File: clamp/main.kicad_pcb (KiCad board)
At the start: 2 copper layers, 76 parts, among them P1 CONN_01X12, P2 CONN_01X15, P3 CONN_01X03, P4 CONN_01X06, Q1 2N3904, U1 LM741, U12 LTZ1000, U13 LM741, U14 LM741, U2 LM741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

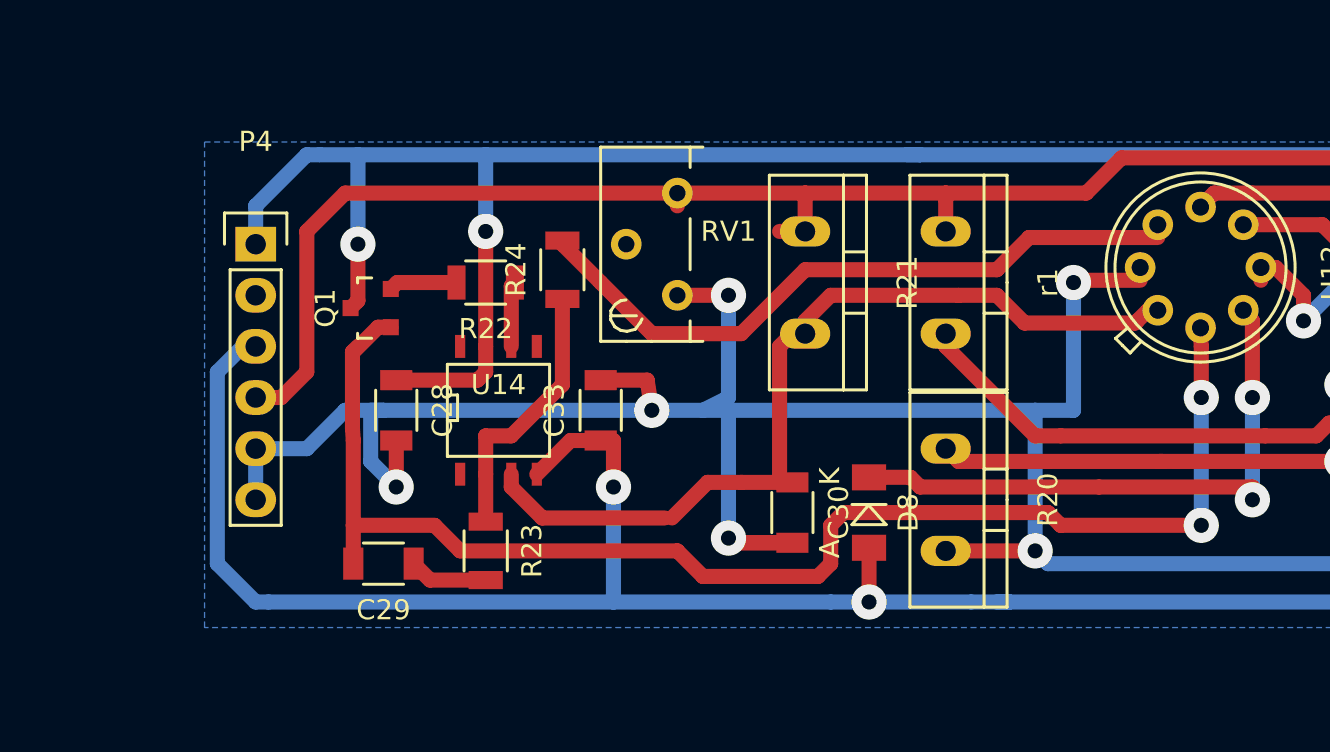
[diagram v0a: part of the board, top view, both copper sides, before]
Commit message: add resistor divider in place of pot
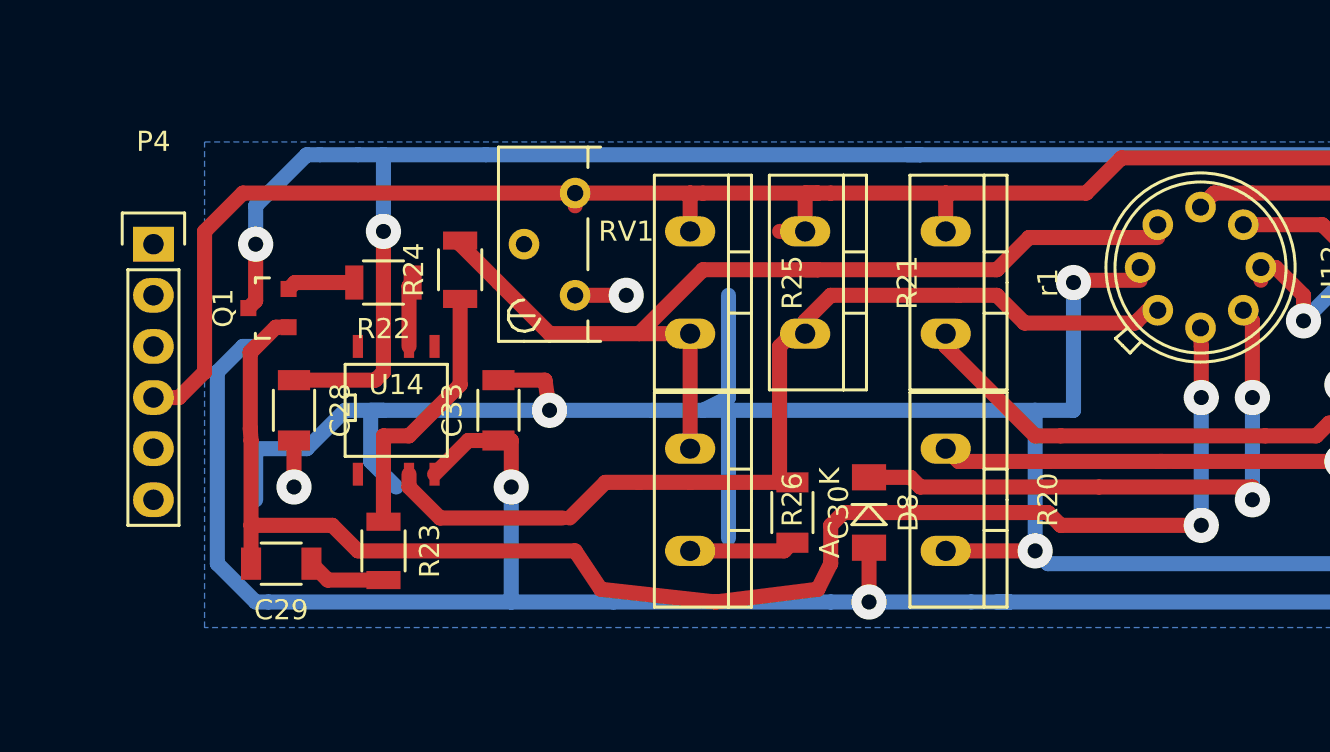
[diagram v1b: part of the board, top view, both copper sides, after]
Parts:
- added R25: 12k, Resistors_ThroughHole:Resistor_TO-220_Vertical, F.Cu at (202.6, 46.4)
- added R26: 1k, Resistors_ThroughHole:Resistor_TO-220_Vertical, F.Cu at (202.6, 57.1)
- moved C28 5.08 mm to (182.9, 52.7)
- moved C33 5.08 mm to (193.0, 52.7)
- moved R22 5.08 mm to (187.3, 46.4)
- moved R23 5.08 mm to (187.3, 59.7)
- moved R24 5.08 mm to (191.1, 45.7)
- moved RV1 5.08 mm to (196.8, 47.0)
- moved C29 5.08 mm to (182.2, 60.3)
- moved P4 5.08 mm to (175.9, 44.5)
- moved Q1 5.08 mm to (181.6, 47.6)
- moved U14 5.08 mm to (188.0, 52.7)
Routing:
- net Net-(R24-Pad2): track 33.6 -> 47.6 mm
- net REF: track 98.1 -> 105.7 mm
- net Net-(C29-Pad2): track 69.1 -> 75.3 mm
- net Net-(C30-Pad1): track 43.4 -> 48.5 mm
- net +VE: track 385.3 -> 380.8 mm
- net GND: track 207.9 -> 207.6 mm, vias 17 -> 16

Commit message: update
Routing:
- net GND: track 207.6 -> 219.7 mm
- net +VE: track 380.8 -> 391.7 mm
- net -VE: track 362.7 -> 365.7 mm
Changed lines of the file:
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@@
   (general
     (links 171)
-    (no_connects 87)
+    (no_connects 82)
     (area -5.909001 -6.355 253.23 151.352002)
     (thickness 1.6)
     (drawings 13)
-    (tracks 524)
+    (tracks 534)
     (zones 0)
     (modules 78)
@@
     (effects (font (size 1.5 1.5) (thickness 0.3)))
   )
+  (segment (start 184.15 40.005) (end 179.07 40.005) (width 0.75) (layer B.Cu) (net 1))
+  (segment (start 175.895 43.18) (end 175.895 44.45) (width 0.75) (layer B.Cu) (net 1))
+  (segment (start 179.07 40.005) (end 175.895 43.18) (width 0.75) (layer B.Cu) (net 1))
   (segment (start 187.325 40.005) (end 187.325 43.815) (width 0.75) (layer B.Cu) (net 1))
   (via (at 187.325 43.815) (size 1.75) (drill 0.75) (layers F.Cu B.Cu) (net 1))
@@
   (via (at 121.92 86.36) (size 1.75) (drill 0.75) (layers F.Cu B.Cu) (net 1))
   (segment (start 121.92 86.36) (end 166.624 86.36) (width 0.75) (layer B.Cu) (net 1))
+  (segment (start 179.07 52.07) (end 179.07 50.165) (width 0.75) (layer B.Cu) (net 2))
+  (segment (start 178.435 49.53) (end 175.895 49.53) (width 0.75) (layer B.Cu) (net 2))
+  (segment (start 179.07 50.165) (end 178.435 49.53) (width 0.75) (layer B.Cu) (net 2))
   (segment (start 193.675 62.23) (end 193.675 56.515) (width 0.75) (layer B.Cu) (net 2))
   (via (at 193.675 56.515) (size 1.75) (drill 0.75) (layers F.Cu B.Cu) (net 2))
   (segment (start 193.675 56.515) (end 193.675 54.205) (width 0.75) (layer F.Cu) (net 2))
-  (segment (start 180.975 49.53) (end 180.34 49.53) (width 0.75) (layer B.Cu) (net 2))
-  (segment (start 180.34 49.53) (end 179.07 50.8) (width 0.75) (layer B.Cu) (net 2))
-  (segment (start 179.07 50.8) (end 179.07 60.325) (width 0.75) (layer B.Cu) (net 2))
+  (segment (start 179.07 50.8) (end 179.07 52.07) (width 0.75) (layer B.Cu) (net 2))
+  (segment (start 179.07 52.07) (end 179.07 60.325) (width 0.75) (layer B.Cu) (net 2))
   (segment (start 179.07 60.325) (end 180.975 62.23) (width 0.75) (layer B.Cu) (net 2))
   (segment (start 180.975 62.23) (end 181.61 62.23) (width 0.75) (layer B.Cu) (net 2))
-  (segment (start 198.755 62.23) (end 193.675 62.23) (width 0.75) (layer B.Cu) (net 2))
+  (segment (start 207.01 62.23) (end 193.675 62.23) (width 0.75) (layer B.Cu) (net 2))
   (segment (start 193.675 62.23) (end 181.61 62.23) (width 0.75) (layer B.Cu) (net 2))
-  (segment (start 209.55 62.23) (end 198.755 62.23) (width 0.75) (layer B.Cu) (net 2))
+  (segment (start 208.28 62.23) (end 207.01 62.23) (width 0.75) (layer B.Cu) (net 2))
   (segment (start 248.92 53.34) (end 248.92 62.23) (width 0.75) (layer F.Cu) (net 2))
   (via (at 248.92 62.23) (size 1.75) (drill 0.75) (layers F.Cu B.Cu) (net 2))
@@
   (segment (start 249.555 52.705) (end 249.555 51.665) (width 0.75) (layer F.Cu) (net 2))
   (segment (start 248.92 53.34) (end 249.555 52.705) (width 0.75) (layer F.Cu) (net 2))
-  (segment (start 211.455 62.23) (end 209.55 62.23) (width 0.75) (layer B.Cu) (net 2))
+  (segment (start 211.455 62.23) (end 208.28 62.23) (width 0.75) (layer B.Cu) (net 2))
   (segment (start 193.675 54.205) (end 191.54 54.205) (width 0.75) (layer F.Cu) (net 2))
   (segment (start 191.54 54.205) (end 189.865 55.88) (width 0.75) (layer F.Cu) (net 2))
@@
   (segment (start 165.862 96.012) (end 165.862 96.52) (width 0.75) (layer B.Cu) (net 2))
   (segment (start 157.132 104.775) (end 160.30194 104.648) (width 0.75) (layer F.Cu) (net 3) (status 30))
+  (segment (start 175.895 46.99) (end 175.26 46.99) (width 0.75) (layer B.Cu) (net 4))
+  (segment (start 175.26 46.99) (end 173.99 48.26) (width 0.75) (layer B.Cu) (net 4))
+  (segment (start 173.99 48.26) (end 173.99 52.705) (width 0.75) (layer B.Cu) (net 4))
+  (segment (start 173.99 52.705) (end 175.895 54.61) (width 0.75) (layer B.Cu) (net 4))
+  (segment (start 175.895 57.15) (end 175.895 54.61) (width 0.75) (layer B.Cu) (net 4))
   (segment (start 202.565 59.69) (end 207.24 59.69) (width 0.75) (layer F.Cu) (net 4))
   (segment (start 207.24 59.69) (end 207.645 59.285) (width 0.75) (layer F.Cu) (net 4))
@@
   (segment (start 217.805 45.72) (end 208.915 45.72) (width 0.75) (layer F.Cu) (net 33))
   (segment (start 191.135 44.45) (end 191.135 44.27) (width 0.75) (layer F.Cu) (net 33))
+  (segment (start 207.645 62.23) (end 209.55 60.325) (width 0.75) (layer F.Cu) (net 34))
+  (segment (start 227.965 58.42) (end 220.98 58.42) (width 0.75) (layer F.Cu) (net 34))
+  (via (at 227.965 52.07) (size 1.75) (drill 0.75) (layers F.Cu B.Cu) (net 34))
+  (segment (start 227.965 58.42) (end 227.965 52.07) (width 0.75) (layer B.Cu) (net 34))
+  (via (at 227.965 58.42) (size 1.75) (drill 0.75) (layers F.Cu B.Cu) (net 34))
+  (segment (start 209.55 60.325) (end 209.55 58.42) (width 0.75) (layer F.Cu) (net 34))
+  (segment (start 209.55 58.42) (end 210.185 57.785) (width 0.75) (layer F.Cu) (net 34))
+  (segment (start 210.185 57.785) (end 211.455 57.785) (width 0.75) (layer F.Cu) (net 34))
+  (segment (start 220.345 57.785) (end 211.455 57.785) (width 0.75) (layer F.Cu) (net 34))
+  (segment (start 220.98 58.42) (end 220.345 57.785) (width 0.75) (layer F.Cu) (net 34))
   (segment (start 182.61076 48.575) (end 181.97576 48.575) (width 0.75) (layer F.Cu) (net 34))
   (segment (start 181.97576 48.575) (end 180.70576 49.845) (width 0.75) (layer F.Cu) (net 34))
@@
   (segment (start 180.745 54.205) (end 180.745 58.42) (width 0.75) (layer F.Cu) (net 34))
   (segment (start 180.70576 53.60924) (end 180.745 54.205) (width 0.75) (layer F.Cu) (net 34))
-  (segment (start 203.835 62.23) (end 208.915 61.595) (width 0.75) (layer F.Cu) (net 34))
+  (segment (start 203.835 62.23) (end 207.645 62.23) (width 0.75) (layer F.Cu) (net 34))
   (segment (start 180.745 58.42) (end 184.785 58.42) (width 0.75) (layer F.Cu) (net 34))
-  (segment (start 208.915 61.595) (end 209.55 60.325) (width 0.75) (layer F.Cu) (net 34))
-  (segment (start 198.12 61.595) (end 203.835 62.23) (width 0.75) (layer F.Cu) (net 34))
-  (segment (start 196.85 59.69) (end 198.12 61.595) (width 0.75) (layer F.Cu) (net 34))
+  (segment (start 198.755 62.23) (end 203.835 62.23) (width 0.75) (layer F.Cu) (net 34))
+  (segment (start 196.85 59.69) (end 198.755 62.23) (width 0.75) (layer F.Cu) (net 34))
   (segment (start 186.055 59.69) (end 196.85 59.69) (width 0.75) (layer F.Cu) (net 34))
   (segment (start 184.785 58.42) (end 186.055 59.69) (width 0.75) (layer F.Cu) (net 34))
   (segment (start 180.745 58.42) (end 180.745 60.325) (width 0.75) (layer F.Cu) (net 34))
-  (segment (start 220.98 58.42) (end 220.345 57.785) (width 0.75) (layer F.Cu) (net 34))
-  (segment (start 220.345 57.785) (end 211.455 57.785) (width 0.75) (layer F.Cu) (net 34))
-  (segment (start 210.185 57.785) (end 211.455 57.785) (width 0.75) (layer F.Cu) (net 34))
-  (segment (start 209.55 58.42) (end 210.185 57.785) (width 0.75) (layer F.Cu) (net 34))
-  (segment (start 209.55 60.325) (end 209.55 58.42) (width 0.75) (layer F.Cu) (net 34))
-  (via (at 227.965 58.42) (size 1.75) (drill 0.75) (layers F.Cu B.Cu) (net 34))
-  (segment (start 227.965 58.42) (end 227.965 52.07) (width 0.75) (layer B.Cu) (net 34))
-  (via (at 227.965 52.07) (size 1.75) (drill 0.75) (layers F.Cu B.Cu) (net 34))
-  (segment (start 227.965 58.42) (end 220.98 58.42) (width 0.75) (layer F.Cu) (net 34))
   (segment (start 227.9275 48.6075) (end 227.9275 48.9325) (width 0.75) (layer F.Cu) (net 34) (status 30))
   (segment (start 227.9275 48.9325) (end 227.965 49.53) (width 0.75) (layer F.Cu) (net 34) (status 10))
@@
     (polygon
       (pts
-        (xy 252.095 63.5) (xy 178.435 63.5) (xy 178.435 39.37) (xy 252.095 39.37)
+        (xy 252.095 63.5) (xy 173.355 63.5) (xy 173.355 39.37) (xy 252.095 39.37)
       )
     )

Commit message: fix bodge
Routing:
- net Net-(R24-Pad2): track 47.6 -> 49.8 mm
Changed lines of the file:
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@@
   (general
     (links 171)
-    (no_connects 82)
-    (area -5.909001 -6.355 253.23 151.352002)
+    (no_connects 81)
+    (area 51.181667 26.645 253.23 151.352002)
     (thickness 1.6)
     (drawings 13)
-    (tracks 534)
+    (tracks 537)
     (zones 0)
     (modules 78)
@@
   (layers
     (0 F.Cu signal)
-    (31 B.Cu signal)
+    (31 B.Cu signal hide)
     (32 B.Adhes user)
     (33 F.Adhes user)
@@
   (segment (start 187.325 61.14) (end 184.56 61.14) (width 0.75) (layer F.Cu) (net 32))
   (segment (start 184.56 61.14) (end 183.745 60.325) (width 0.75) (layer F.Cu) (net 32))
-  (segment (start 202.565 48.895) (end 202.565 54.61) (width 0.75) (layer F.Cu) (net 33))
+  (segment (start 194.31 44.45) (end 191.315 44.45) (width 0.75) (layer F.Cu) (net 33) (status C00000))
+  (segment (start 191.315 44.45) (end 191.135 44.27) (width 0.75) (layer F.Cu) (net 33) (status C00000))
   (segment (start 200.025 48.895) (end 202.565 48.895) (width 0.75) (layer F.Cu) (net 33))
+  (segment (start 202.565 48.895) (end 202.565 46.355) (width 0.75) (layer F.Cu) (net 33))
+  (segment (start 202.565 48.895) (end 202.565 54.61) (width 0.75) (layer F.Cu) (net 33))
   (segment (start 208.915 45.72) (end 203.2 45.72) (width 0.75) (layer F.Cu) (net 33))
+  (segment (start 202.565 46.355) (end 203.2 45.72) (width 0.75) (layer F.Cu) (net 33))
   (segment (start 208.915 45.72) (end 208.28 45.72) (width 0.75) (layer F.Cu) (net 33))
   (segment (start 193.04 46.355) (end 191.135 44.45) (width 0.75) (layer F.Cu) (net 33))
   (segment (start 195.58 48.895) (end 200.025 48.895) (width 0.75) (layer F.Cu) (net 33))
-  (segment (start 200.025 48.895) (end 203.2 45.72) (width 0.75) (layer F.Cu) (net 33))
   (segment (start 193.04 46.355) (end 195.58 48.895) (width 0.75) (layer F.Cu) (net 33))
   (segment (start 225.8025 44.1175) (end 219.4075 44.1175) (width 0.75) (layer F.Cu) (net 33) (status 10))

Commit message: update
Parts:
- removed RV1: POT, Potentiometers:Potentiometer_Bourns_3296Y_3-8Zoll_Angular_ScrewUp
- added C31: 0.1uF, Capacitors_SMD:C_1206, F.Cu at (244.5, 50.2)
- added C32: 0.1uF, Capacitors_SMD:C_1206, F.Cu at (205.7, 52.7)
- C27, C33: value C -> 10uF
- C28, C34: value C -> 0.1uF
- P4: value CONN_01X06 -> CONN_01X08; footprint Pin_Headers:Pin_Header_Straight_1x06 -> Pin_Headers:Pin_Header_Straight_1x08
- moved C27 44.8 mm to (196.8, 38.1)
- moved r1 27.0 mm to (241.3, 39.4), turned to 180 degrees
- moved R20 23.7 mm to (237.5, 48.9)
- moved R21 21.5 mm to (226.1, 58.4), turned to 90 degrees
- moved D8 19.8 mm to (231.1, 55.9)
- moved R26 16.8 mm to (210.8, 42.5)
- moved R25 15.4 mm to (212.1, 58.4), turned to 90 degrees
- moved C28 12.7 mm to (195.6, 52.7)
- moved R22 12.7 mm to (200.0, 46.4)
- moved R23 12.7 mm to (200.0, 59.7)
- moved R24 12.7 mm to (203.8, 45.7)
- moved C29 12.7 mm to (194.9, 60.3)
- moved Q1 12.7 mm to (194.3, 47.6)
- moved U14 12.7 mm to (200.7, 52.7)
- moved C30 11.9 mm to (219.1, 54.6), turned to 90 degrees
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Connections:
- D8 pad 2: -VE -> GND-H
- P4 pad 5: GND -> GND-H
- R25 pad 2: Net-(R24-Pad2) -> (no net)
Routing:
- net GND: track 219.7 -> 106.8 mm, vias 16 -> 11
- net (no net): track 0.00 -> 76.0 mm, vias 0 -> 1
- net Net-(C29-Pad2): track 75.4 -> 30.3 mm, vias 2 -> 0
- net REF: track 105.7 -> 69.8 mm, vias 2 -> 0
- net Net-(R24-Pad2): track 49.8 -> 23.8 mm
- net Net-(D8-Pad1): track 29.6 -> 13.9 mm, vias 2 -> 0
- net +VE: track 391.7 -> 405.5 mm, vias 10 -> 9
- net Net-(C30-Pad1): track 48.5 -> 41.2 mm
- net Net-(R20-Pad1): track 47.7 -> 41.4 mm
- net GND-H: track 0.00 -> 6.04 mm
- net -VE: track 365.7 -> 369.3 mm, vias 11 -> 9
- net Net-(C26-Pad1): track 59.5 -> 56.5 mm

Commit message: update
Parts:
- added R28: 0, Resistors_SMD:R_1206, F.Cu at (191.8, 59.1)
- moved C33 14.8 mm to (204.5, 64.8)
- moved R25 11.5 mm to (210.8, 47.0)
- moved R21 8.03 mm to (233.7, 55.9), turned to 270 degrees
- moved R24 7.10 mm to (202.6, 38.7)
- moved R20 4.26 mm to (239.4, 52.7)
- moved R26 3.86 mm to (210.2, 38.7), turned to 0 degrees
- moved D7 2.29 mm to (248.3, 43.2), turned to 180 degrees
- moved D8 2.29 mm to (229.9, 57.8)
- moved P4 2.01 mm to (188.0, 45.1)
- moved C34 2.01 mm to (255.3, 52.1)
- moved R23 1.91 mm to (200.0, 61.6)
- moved C29 1.80 mm to (196.2, 61.6), turned to 90 degrees
- moved C27 0.63 mm to (196.8, 38.7)
- moved C30 0.63 mm to (219.1, 54.0)
- moved r1 0.63 mm to (241.3, 38.7)
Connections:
- R25 pad 2: (no net) -> Net-(R24-Pad2)
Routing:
- net (no net): track 76.0 -> 3.40 mm, vias 1 -> 0
- net Net-(C29-Pad2): track 30.3 -> 73.7 mm, vias 0 -> 2
- net Net-(C30-Pad1): track 41.2 -> 69.8 mm
- net REF: track 69.8 -> 43.7 mm
- net GND-H: track 6.04 -> 29.5 mm
- net Net-(R23-Pad1): track 13.8 -> 23.3 mm
- net Net-(R20-Pad1): track 41.4 -> 34.6 mm
- net +VE: track 405.5 -> 399.6 mm
- net GND: track 106.8 -> 101.0 mm, vias 11 -> 18
- net -VE: track 369.3 -> 373.9 mm, vias 9 -> 10
- net Net-(R24-Pad2): track 23.8 -> 27.2 mm
- net Net-(C26-Pad1): track 56.5 -> 55.2 mm
- net Net-(D8-Pad1): track 13.9 -> 14.9 mm

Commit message: update
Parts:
- moved C33 8.03 mm to (212.1, 62.2), turned to 0 degrees
- moved R28 6.35 mm to (191.8, 52.7), turned to 270 degrees
- moved C34 3.18 mm to (253.4, 54.6), turned to 270 degrees
- moved D8 1.91 mm to (228.0, 57.8)
- moved R21 1.27 mm to (232.4, 55.9)
- moved C29 1.27 mm to (196.2, 60.3)
- moved R23 1.27 mm to (200.0, 60.3)
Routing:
- net GND-H: track 29.5 -> 57.2 mm
- net Net-(D8-Pad1): track 14.9 -> 22.2 mm
- net REF: track 43.7 -> 37.5 mm
- net (no net): track 3.40 -> 0.23 mm
- net Net-(R24-Pad2): track 27.2 -> 29.3 mm
- net +VE: track 399.6 -> 397.5 mm
- net Net-(C29-Pad2): track 73.7 -> 72.2 mm
- net Net-(R23-Pad1): track 23.3 -> 22.0 mm
- net Net-(C30-Pad1): track 69.8 -> 68.5 mm
- net GND: track 101.0 -> 101.7 mm, vias 18 -> 19
- net Net-(C26-Pad1): track 55.2 -> 54.7 mm
- net Net-(R20-Pad1): track 34.6 -> 34.0 mm
- net -VE: track 373.9 -> 373.4 mm, vias 10 -> 11
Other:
- net class Default: via_dia 1.75 -> 1.5

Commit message: update
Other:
- net class Default: via_dia 1.5 -> 1.75

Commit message: update
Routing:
- net Net-(C30-Pad1): track 68.5 -> 65.9 mm
- net REF: track 37.5 -> 36.5 mm
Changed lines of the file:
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@@
     (thickness 1.6)
     (drawings 13)
-    (tracks 518)
+    (tracks 510)
     (zones 0)
     (modules 80)
@@
     (effects (font (size 1.5 1.5) (thickness 0.3)))
   )
-  (segment (start 243.84 42.4325) (end 243.84 42.545) (width 0.75) (layer F.Cu) (net 0))
-  (segment (start 243.84 42.545) (end 243.84 42.4325) (width 0.75) (layer F.Cu) (net 0))
   (segment (start 194.945 34.925) (end 193.675 36.195) (width 0.75) (layer F.Cu) (net 1))
   (segment (start 193.675 36.195) (end 193.675 36.83) (width 0.75) (layer F.Cu) (net 1))
@@
   (segment (start 149.352 85.852) (end 149.352 88.9) (width 0.75) (layer F.Cu) (net 5))
   (segment (start 149.479 89.027) (end 149.987 89.535) (width 0.75) (layer F.Cu) (net 5))
+  (segment (start 243.84 38.735) (end 243.84 43.18) (width 0.75) (layer F.Cu) (net 6))
   (segment (start 232.41 48.895) (end 232.41 43.18) (width 0.75) (layer F.Cu) (net 6))
   (segment (start 235.585 43.18) (end 232.41 43.18) (width 0.75) (layer F.Cu) (net 6))
@@
   (segment (start 232.41 48.26) (end 232.41 48.895) (width 0.75) (layer F.Cu) (net 6))
   (segment (start 232.41 48.895) (end 232.41 53.34) (width 0.75) (layer F.Cu) (net 6))
-  (segment (start 243.84 38.735) (end 243.84 43.18) (width 0.75) (layer F.Cu) (net 6))
   (segment (start 246.53494 43.18) (end 243.84 43.18) (width 0.75) (layer F.Cu) (net 6))
-  (segment (start 245.78744 42.4325) (end 246.53494 43.18) (width 0.75) (layer F.Cu) (net 6))
   (segment (start 227.1175 42.4325) (end 227.2175 42.4325) (width 0.75) (layer F.Cu) (net 6))
   (segment (start 227.1175 42.4325) (end 227.8525 42.4325) (width 0.75) (layer F.Cu) (net 6))
@@
   (segment (start 222.25 57.785) (end 219.075 57.785) (width 0.75) (layer F.Cu) (net 36))
   (segment (start 219.075 57.785) (end 202.565 57.785) (width 0.75) (layer F.Cu) (net 36))
-  (segment (start 202.565 57.785) (end 202.565 57.419998) (width 0.75) (layer F.Cu) (net 36))
   (segment (start 221.9925 55.88) (end 221.9925 57.419998) (width 0.75) (layer F.Cu) (net 36))
-  (segment (start 202.565 57.419998) (end 202.295002 57.419998) (width 0.75) (layer F.Cu) (net 36))
-  (segment (start 202.295002 57.419998) (end 201.295 56.419996) (width 0.75) (layer F.Cu) (net 36))
   (segment (start 201.295 56.419996) (end 201.295 56.515) (width 0.75) (layer F.Cu) (net 36))
   (segment (start 219.075 55.475) (end 219.075 57.419998) (width 0.75) (layer F.Cu) (net 36) (status 10))
@@
   (segment (start 218.845 55.475) (end 219.075 55.475) (width 0.75) (layer F.Cu) (net 36) (status 30))
   (segment (start 221.9925 49.53) (end 221.9925 55.88) (width 0.75) (layer F.Cu) (net 36))
-  (segment (start 221.9925 55.88) (end 222.25 55.88) (width 0.75) (layer F.Cu) (net 36))
   (segment (start 221.9925 44.5575) (end 221.9925 49.53) (width 0.75) (layer F.Cu) (net 36))
   (segment (start 221.9925 49.53) (end 221.9925 49.7875) (width 0.75) (layer F.Cu) (net 36))
-  (segment (start 218.845 55.245) (end 219.075 55.475) (width 0.75) (layer F.Cu) (net 36) (status 30))
   (segment (start 232.6675 58.6775) (end 232.41 58.42) (width 0.75) (layer F.Cu) (net 36) (status 30))
   (segment (start 232.6675 58.6775) (end 232.41 58.42) (width 0.75) (layer B.Cu) (net 36) (status 30))
